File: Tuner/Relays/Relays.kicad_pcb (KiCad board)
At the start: 2 copper layers, 100 x 100 mm, 82 parts, among them J1 Conn_01x03, J10 Conn_01x02, J11 Conn_01x02, J12 Conn_01x01, J13 Conn_01x01, J14 Conn_01x01, J15 Conn_01x01, J16 Conn_01x02, J17 Conn_02x10_Odd_Even, J18 Conn_01x02, J19 Conn_01x03, J2 Conn_01x03, J3 Conn_01x03, J4 Conn_01x03, J5 Conn_01x03, J6 Conn_01x03, J7 Conn_01x03, J8 Conn_01x02, J9 Conn_01x02

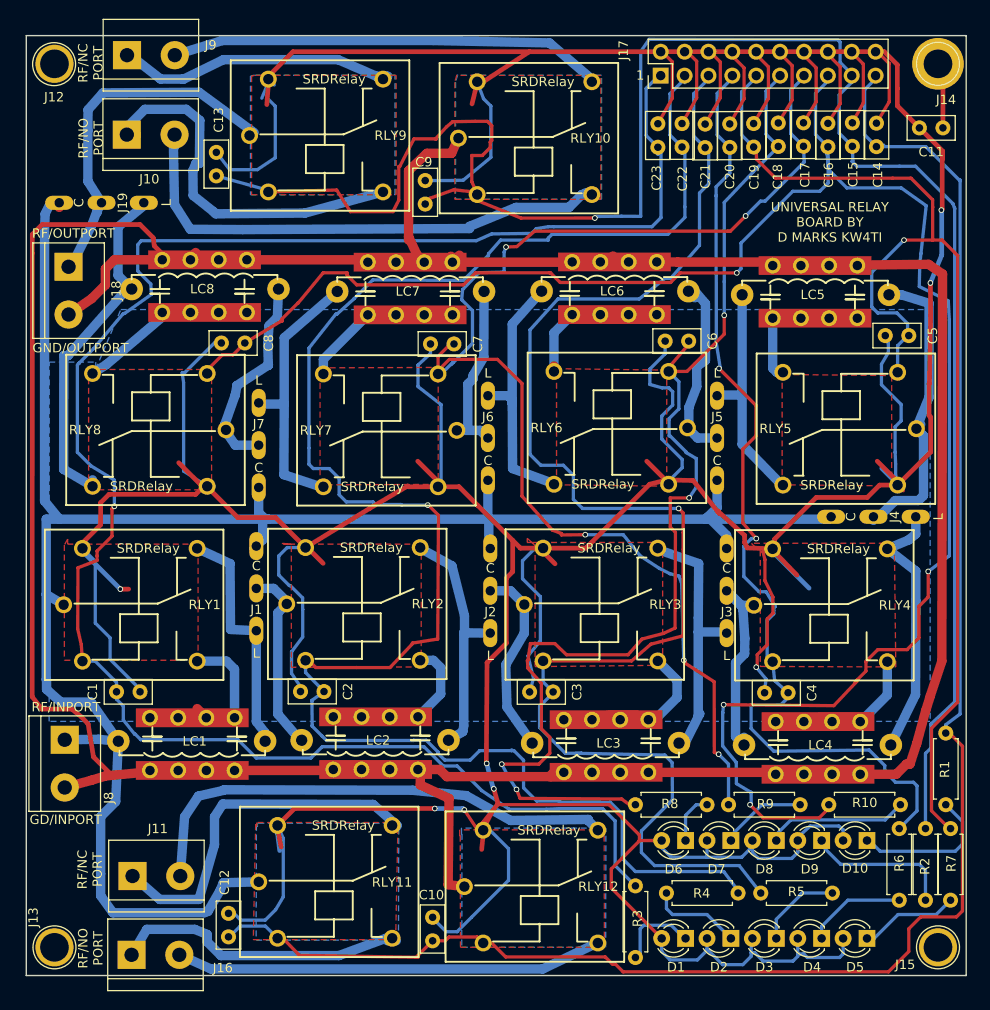
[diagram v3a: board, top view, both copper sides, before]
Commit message: Relay boards changed to have coil terminals all on same side
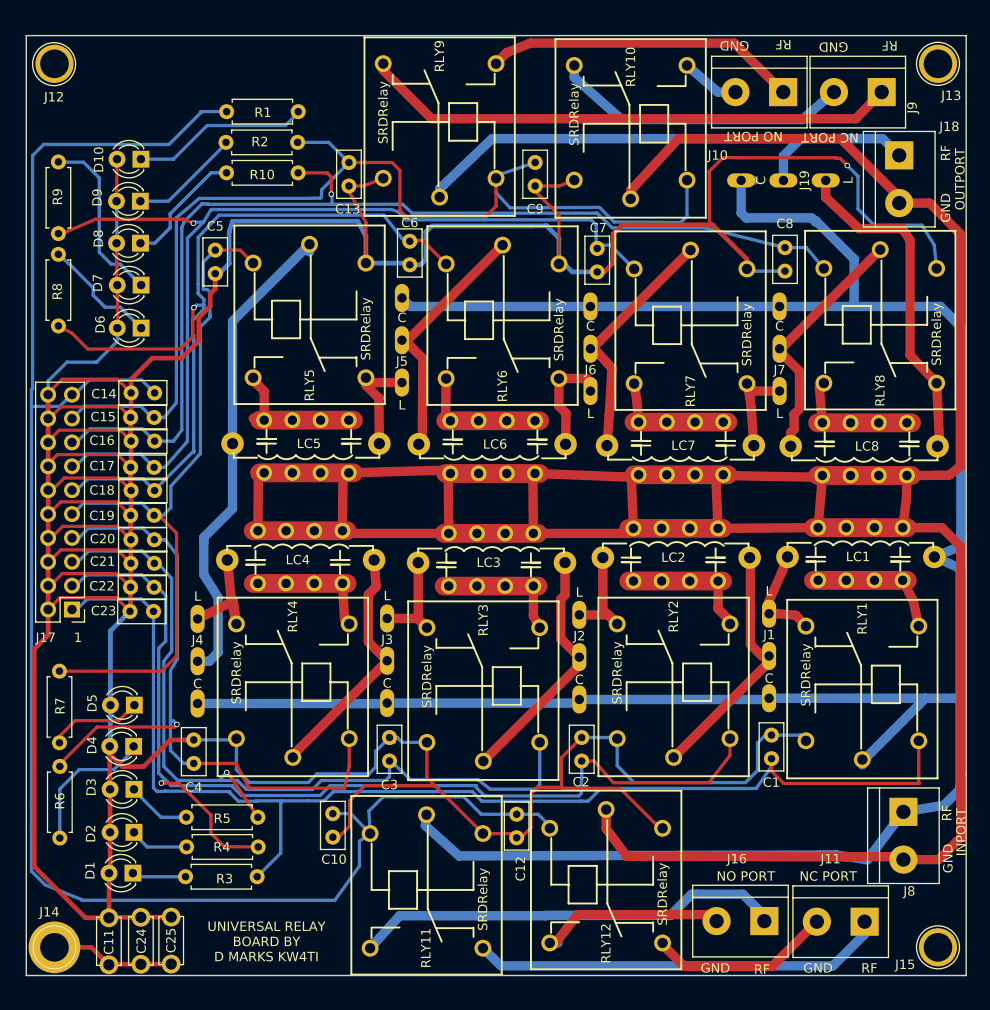
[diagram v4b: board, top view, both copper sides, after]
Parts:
- added C24: 10 nF, Capacitors_THT:C_Disc_D5.0mm_W2.5mm_P5.00mm, F.Cu at (62.2, 148.8)
- added C25: 10 nF, Capacitors_THT:C_Disc_D5.0mm_W2.5mm_P5.00mm, F.Cu at (65.4, 148.8)
- C11: footprint Capacitors_THT:C_Disc_D5.0mm_W2.5mm_P2.50mm -> Capacitors_THT:C_Disc_D5.0mm_W2.5mm_P5.00mm
- moved J13 132.9 mm to (147.0, 53.0)
- moved J14 132.9 mm to (53.0, 147.0)
- moved C11 125.7 mm to (58.8, 148.9), turned to 90 degrees
- moved R2 109.7 mm to (71.2, 61.4), turned to 0 degrees
- moved D10 105.9 mm to (62.2, 63.1)
- moved R9 104.4 mm to (53.4, 63.4), turned to 270 degrees
- moved R1 100.9 mm to (78.9, 58.1), turned to 180 degrees
- moved D9 99.4 mm to (62.1, 67.6)
- moved R10 98.3 mm to (71.3, 64.6), turned to 0 degrees
- moved R7 96.3 mm to (53.5, 125.2)
- moved D8 92.8 mm to (62.1, 72.1)
- moved R8 90.5 mm to (53.4, 73.3), turned to 270 degrees
- moved J8 89.6 mm to (143.3, 132.6)
- moved R6 89.6 mm to (53.6, 135.4)
- moved J18 89.2 mm to (142.9, 62.7)
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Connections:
- net BYPASS renamed Net-(LC1-Pad1)
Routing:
- net +5V: track 742.9 -> 560.7 mm, vias 8 -> 1
- net RLY9: track 209.4 -> 116.2 mm, vias 1 -> 0
- net RLY8: track 203.3 -> 113.6 mm, vias 4 -> 1
- net RFSIG: track 218.0 -> 296.0 mm
- net RLY2: track 191.3 -> 116.4 mm
- net RLY1: track 202.8 -> 130.6 mm, vias 1 -> 0
- net RLY3: track 154.7 -> 88.6 mm
- net Net-(J10-Pad2): track 57.4 -> 6.21 mm
- net RLY5: track 124.2 -> 76.6 mm, vias 1 -> 0
- net RLY6: track 128.6 -> 89.5 mm, vias 4 -> 1
- net RLY7: track 139.0 -> 105.0 mm, vias 5 -> 1
- net Net-(J11-Pad2): track 52.8 -> 19.5 mm
- net RLY4: track 108.3 -> 76.1 mm, vias 2 -> 1
- net Net-(J9-Pad1): track 30.8 -> 57.1 mm
- net Net-(J16-Pad2): track 45.7 -> 20.1 mm
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- removed copper zone on B.Cu, net +5V
- removed copper zone on F.Cu, net +5V
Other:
- board text added: "GND"
- board text added: "INPORT"
- board text added: "NC PORT"
- board text added: "NO PORT"
- board text added: "OUTPORT"
- board text added: "RF"
- board text removed: "GD/INPORT"
- board text removed: "GND/OUTPORT"
- board text removed: "RF/INPORT"
- board text removed: "RF/NC PORT"
- board text removed: "RF/NO PORT"
- board text removed: "RF/OUTPORT"

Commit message: Added boards for SMIH/Schrack Relays
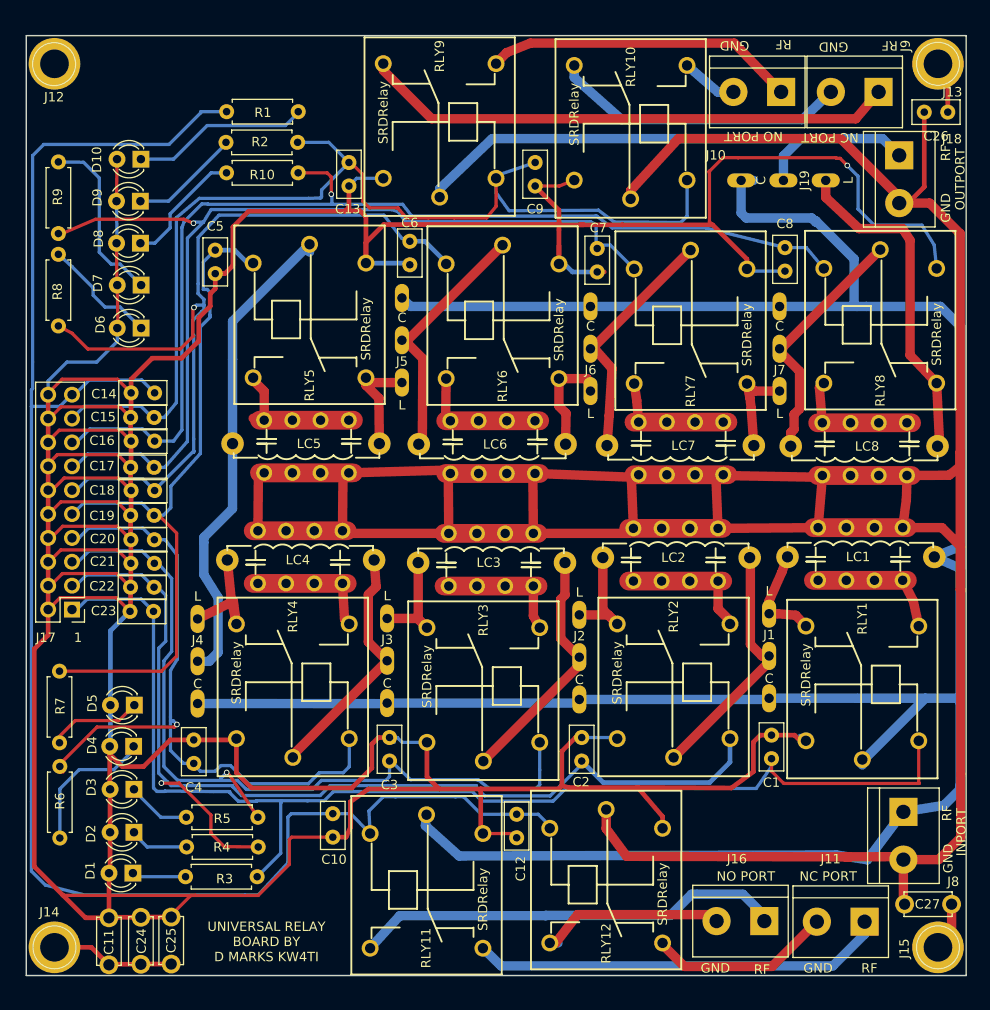
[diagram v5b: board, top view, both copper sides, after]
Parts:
- added C26: 10 nF, Capacitors_THT:C_Disc_D5.0mm_W2.5mm_P2.50mm, F.Cu at (148.0, 58.1)
- added C27: 10 nF, Capacitors_THT:C_Disc_D5.0mm_W2.5mm_P5.00mm, F.Cu at (148.4, 142.4)
- moved J9 0.33 mm to (140.7, 56.0)
- moved J10 0.22 mm to (130.3, 56.0)
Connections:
- J13 pad 1: (no net) -> Net-(C26-Pad1)
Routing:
- net +5V: track 560.7 -> 601.1 mm
- net RFGND: track 282.7 -> 313.5 mm
- net Net-(C26-Pad1): track 0.00 -> 5.57 mm
- net Net-(C27-Pad1): track 0.00 -> 5.19 mm
- net RLY10: track 184.1 -> 181.7 mm
- net RLY2: track 116.4 -> 114.8 mm
- net RLY4: track 76.1 -> 74.9 mm
